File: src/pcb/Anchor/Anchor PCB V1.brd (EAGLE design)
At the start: 100.1 x 68.7 mm, 85 parts, among them IC1 ENC28J60-I_SS, IC2 TPS23750PWP, IC3 MIC5219-3.3YM5-TR, IC4 DWM1000, J1 0826-1X1T-GJ-F, J2 105017-0001, Q1 32 MHz, Q2 SUD06N10-225L, U1 ATSAMD21G-A, Y1 25 MHz

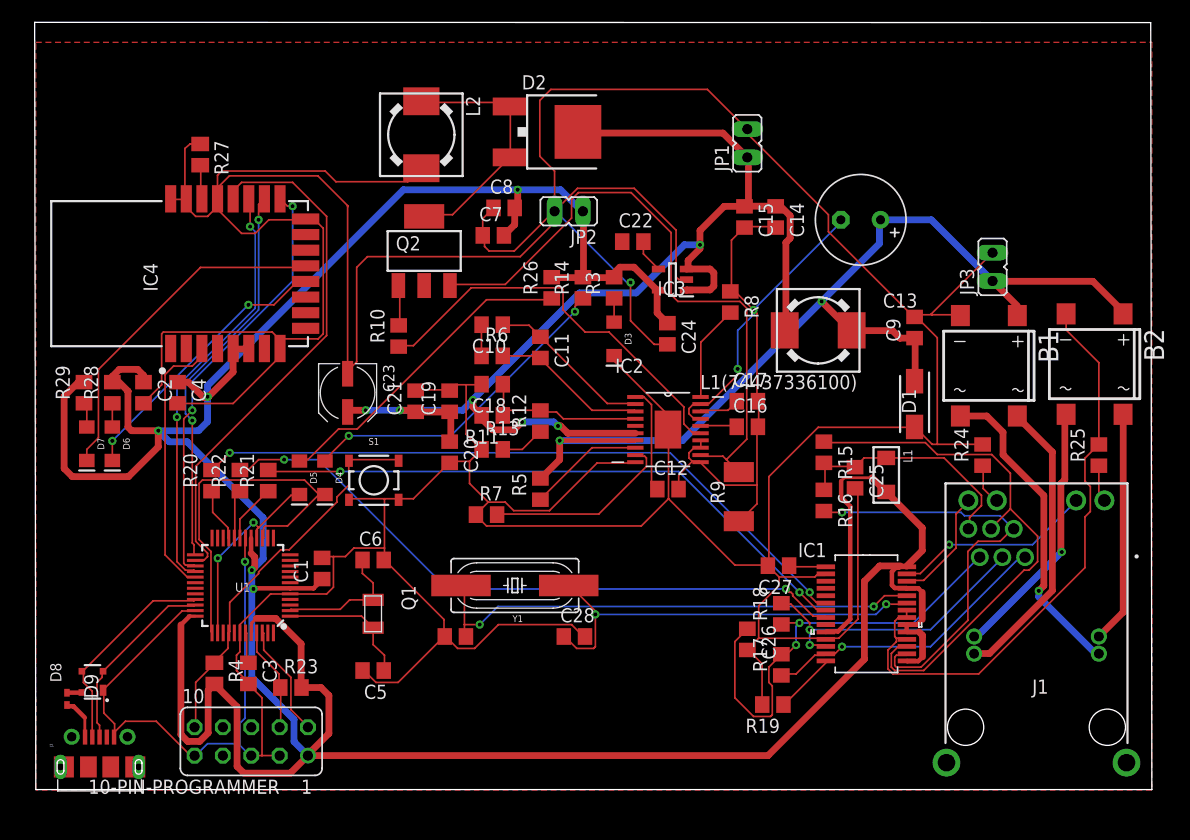
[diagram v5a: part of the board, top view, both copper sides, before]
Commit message: Added mounting holes
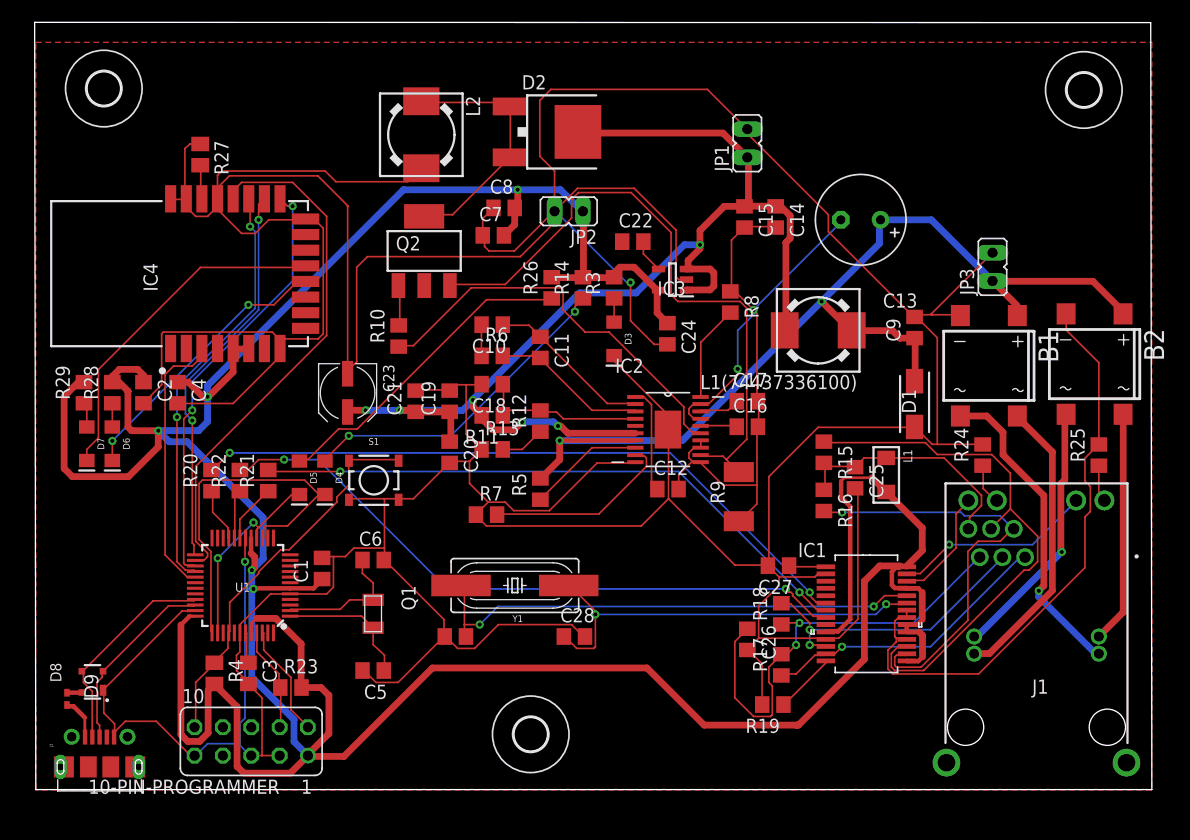
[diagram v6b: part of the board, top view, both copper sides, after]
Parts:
- added H1, H2, H3: MOUNT-HOLE3.0, holes:3,0
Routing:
- net VCC: track 325.2 -> 329.5 mm
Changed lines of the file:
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@@
 <layer number="43" name="vRestrict" color="2" fill="10" visible="yes" active="yes"/>
 <layer number="44" name="Drills" color="7" fill="1" visible="no" active="yes"/>
-<layer number="45" name="Holes" color="7" fill="1" visible="no" active="yes"/>
+<layer number="45" name="Holes" color="7" fill="1" visible="yes" active="yes"/>
 <layer number="46" name="Milling" color="3" fill="1" visible="no" active="yes"/>
 <layer number="47" name="Measures" color="7" fill="1" visible="no" active="yes"/>
@@
 <attribute name="VALUE" x="54.0512" y="42.1132" size="1.27" layer="27" rot="R270"/>
 </element>
+<element name="H1" library="holes" library_urn="urn:adsk.eagle:library:237" package="3,0" package3d_urn="urn:adsk.eagle:package:14277/1" value="MOUNT-HOLE3.0" x="44.3484" y="4.953" smashed="yes"/>
+<element name="H2" library="holes" library_urn="urn:adsk.eagle:library:237" package="3,0" package3d_urn="urn:adsk.eagle:package:14277/1" value="MOUNT-HOLE3.0" x="6.096" y="62.8142" smashed="yes"/>
+<element name="H3" library="holes" library_urn="urn:adsk.eagle:library:237" package="3,0" package3d_urn="urn:adsk.eagle:package:14277/1" value="MOUNT-HOLE3.0" x="93.9038" y="62.6872" smashed="yes"/>
 </elements>
 <signals>
@@
 <wire x1="78.0288" y1="20.0152" x2="79.4258" y2="21.4122" width="0.6096" layer="1"/>
 <wire x1="74.2442" y1="11.684" x2="74.2442" y2="18.669" width="0.6096" layer="1"/>
-<wire x1="65.6082" y1="3.048" x2="74.2442" y2="11.684" width="0.6096" layer="1"/>
-<wire x1="24.384" y1="3.048" x2="65.6082" y2="3.048" width="0.6096" layer="1"/>
 <via x="19.3548" y="19.6596" extent="1-16" drill="0.35"/>
 <via x="19.5072" y="17.9832" extent="1-16" drill="0.35"/>
 <via x="15.3924" y="35.2044" extent="1-16" drill="0.35"/>
 <via x="10.9728" y="32.1564" extent="1-16" drill="0.35"/>
+<wire x1="68.1736" y1="5.7658" x2="68.1863" y2="5.7785" width="0.6096" layer="1"/>
+<wire x1="68.3387" y1="5.7785" x2="74.2442" y2="11.684" width="0.6096" layer="1"/>
 <wire x1="77.08140625" y1="19.9009" x2="77.3303" y2="19.9009" width="0.4064" layer="1"/>
 <wire x1="77.3303" y1="19.9009" x2="77.47" y2="20.0406" width="0.4064" layer="1"/>
@@
 <wire x1="56.5912" y1="41.7932" x2="55.6714" y2="42.713" width="0.6096" layer="1"/>
 <wire x1="55.6714" y1="42.713" x2="55.6714" y2="44.7446" width="0.6096" layer="1"/>
+<wire x1="68.3387" y1="5.7785" x2="68.1863" y2="5.7785" width="0.6096" layer="1"/>
+<wire x1="68.1863" y1="5.7785" x2="59.8805" y2="5.7785" width="0.6096" layer="1"/>
+<wire x1="35.5346" y1="10.8966" x2="27.6098" y2="2.9718" width="0.6096" layer="1"/>
+<wire x1="27.6098" y1="2.9718" x2="24.4602" y2="2.9718" width="0.6096" layer="1"/>
+<wire x1="24.4602" y1="2.9718" x2="24.384" y2="3.048" width="0.6096" layer="1"/>
+<wire x1="59.8805" y1="5.7785" x2="54.7624" y2="10.8966" width="0.6096" layer="1"/>
+<wire x1="54.7624" y1="10.8966" x2="35.5346" y2="10.8966" width="0.6096" layer="1"/>
 <wire x1="15.4178" y1="35.179" x2="15.4432" y2="35.179" width="0" layer="19" extent="1-1"/>
 <wire x1="6.858" y1="36.51" x2="7.4066" y2="36.5608" width="0" layer="19" extent="1-1"/>

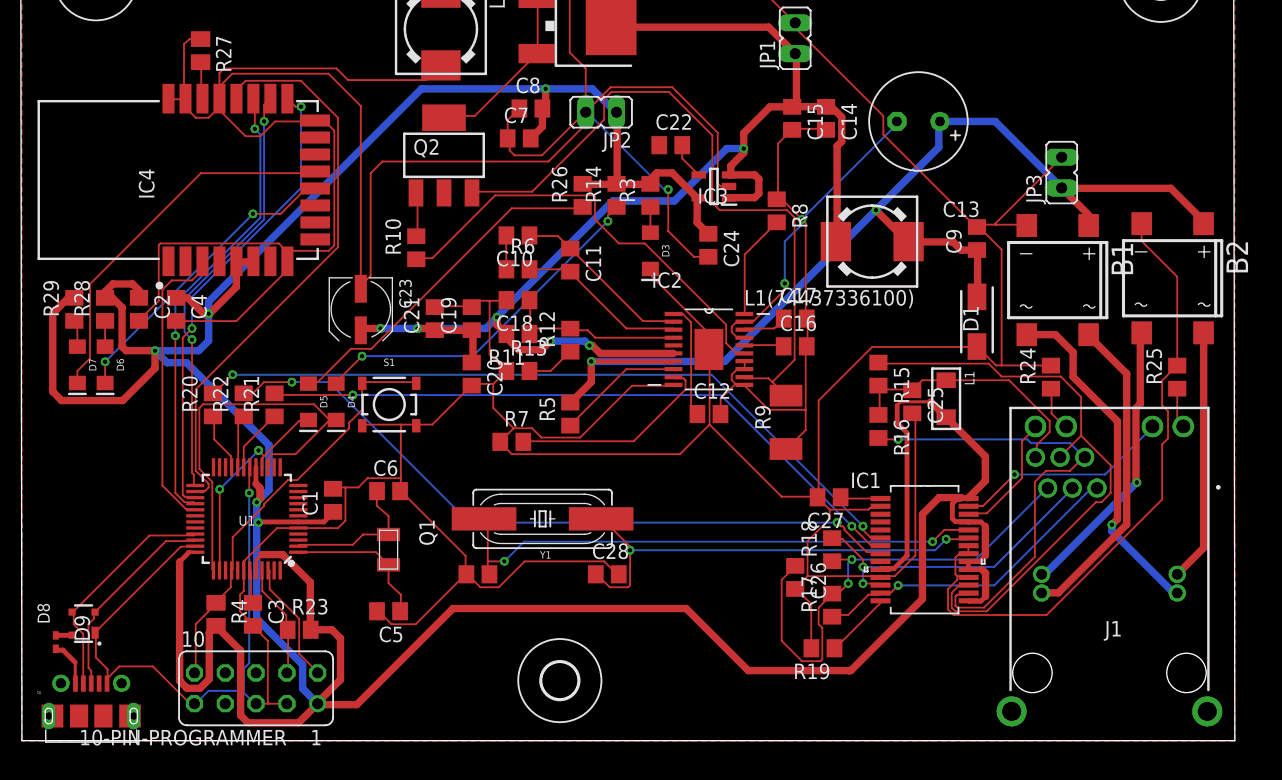
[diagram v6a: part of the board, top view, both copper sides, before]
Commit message: Bug fixes ground plane
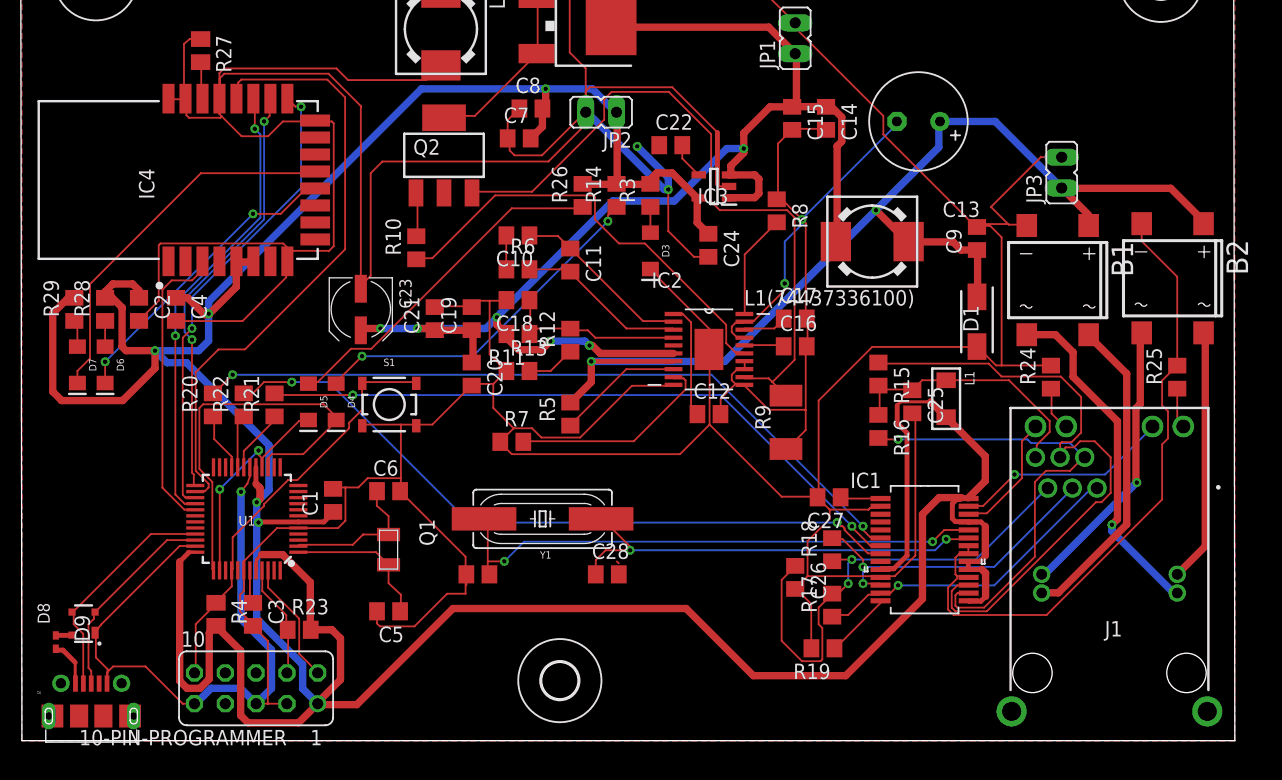
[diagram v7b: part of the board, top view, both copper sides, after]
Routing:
- net SCK2_MC: track 47.7 -> 51.2 mm
- net TPOUT+: track 49.5 -> 52.7 mm
- net GND: track 615.6 -> 617.7 mm, vias 2 -> 3
- net OSC1: track 38.2 -> 36.3 mm
- net TX_MC: track 33.6 -> 34.7 mm
- net VCC: track 329.5 -> 330.4 mm
- net VBUS: track 3.39 -> 3.95 mm
- net USB-: track 18.8 -> 19.3 mm
